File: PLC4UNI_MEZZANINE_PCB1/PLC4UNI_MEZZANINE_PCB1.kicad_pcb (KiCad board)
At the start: 2 copper layers, 29.7 x 37.1 mm, 15 parts, among them J1 PZ254R-12-14P, U1 MC-121-L119

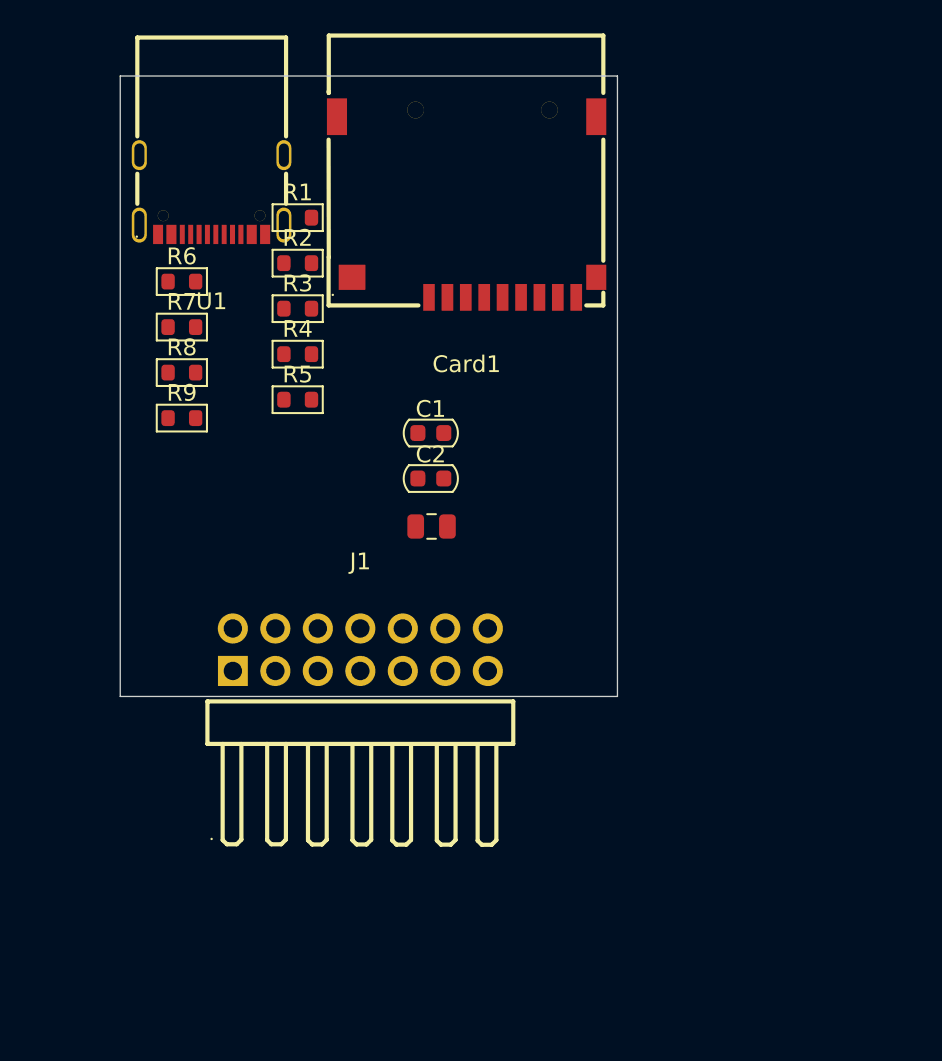
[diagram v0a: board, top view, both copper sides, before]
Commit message: Se cambio el conector J1 de 16 pines por un conector de 18 pines, para poder utilizar el display + touch en modo spi.
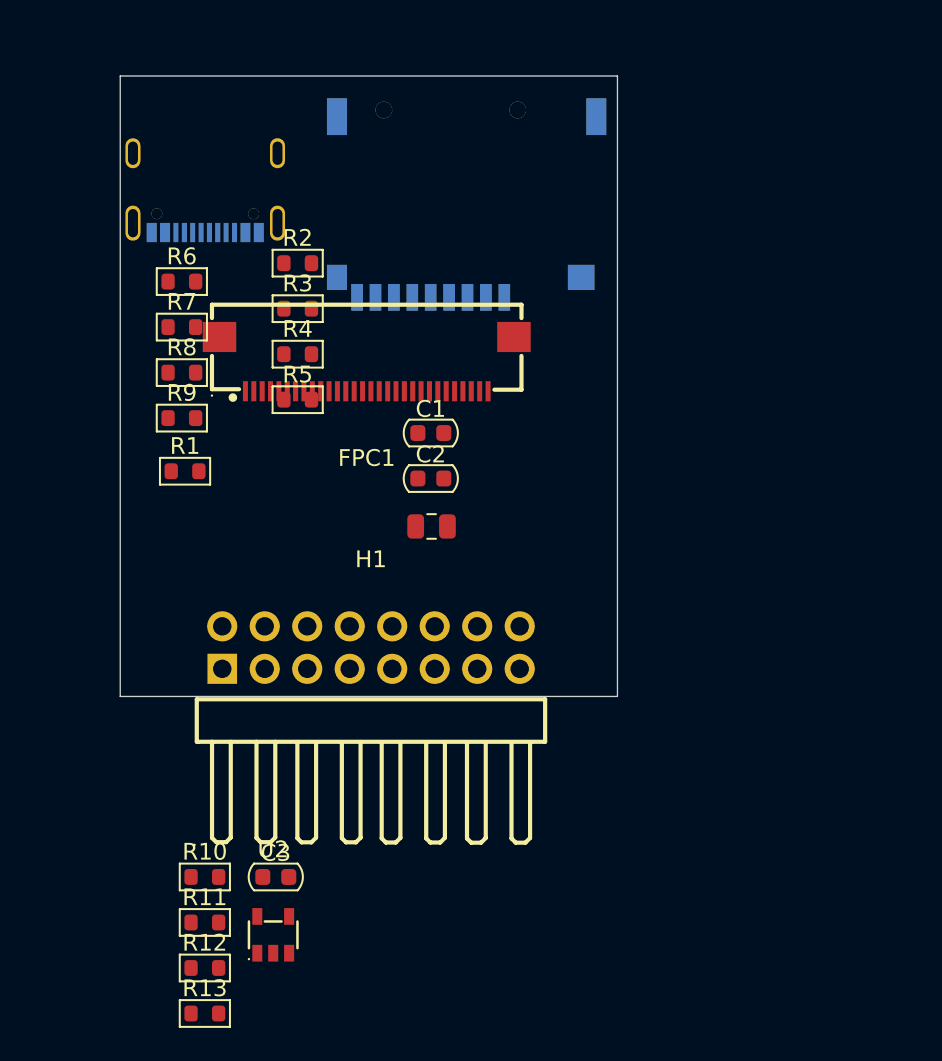
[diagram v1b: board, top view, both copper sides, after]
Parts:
- removed J1: PZ254R-12-14P, EasyEDA:HDR-TH_14P-P2.54-H-M-R2-C7-S2.54
- added C3: 10uF, Capacitor_SMD_AKL:C_0603_1608Metric, F.Cu at (107.6, 112.0)
- added FPC1: FPC-05FB-30PH20, EasyEDA:FPC-SMD_30P-P0.50_FPC-05FB-30PH20, F.Cu at (113.0, 81.4)
- added H1: PZ254R-12-16P, EasyEDA:HDR-TH_16P-P2.54-H-M-R2-C8-S2.54, F.Cu at (113.3, 98.3)
- added R10: 6.8K, Resistor_SMD_AKL:R_0603_1608Metric, F.Cu at (103.4, 112.0)
- added R11: 300, Resistor_SMD_AKL:R_0603_1608Metric, F.Cu at (103.4, 114.7)
- added R12: 5.1k, Resistor_SMD_AKL:R_0603_1608Metric, F.Cu at (103.4, 117.4)
- added R13: 5.1k, Resistor_SMD_AKL:R_0603_1608Metric, F.Cu at (103.4, 120.2)
- added U2: MT9700-N, EasyEDA:SOT-23-5_L2.9-W1.6-P0.95-LS2.9-BL, F.Cu at (107.4, 115.5)
- Card1, U1: moved to B.Cu
- moved R1 16.6 mm to (102.2, 87.8)
- moved U1 0.40 mm to (103.4, 71.1), turned to 0 degrees
- turned Card1 to 0 degrees
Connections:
- net Net-(Card1-CD/DAT3) renamed /sd_cs

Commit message: Avances en esquemas y documentacion
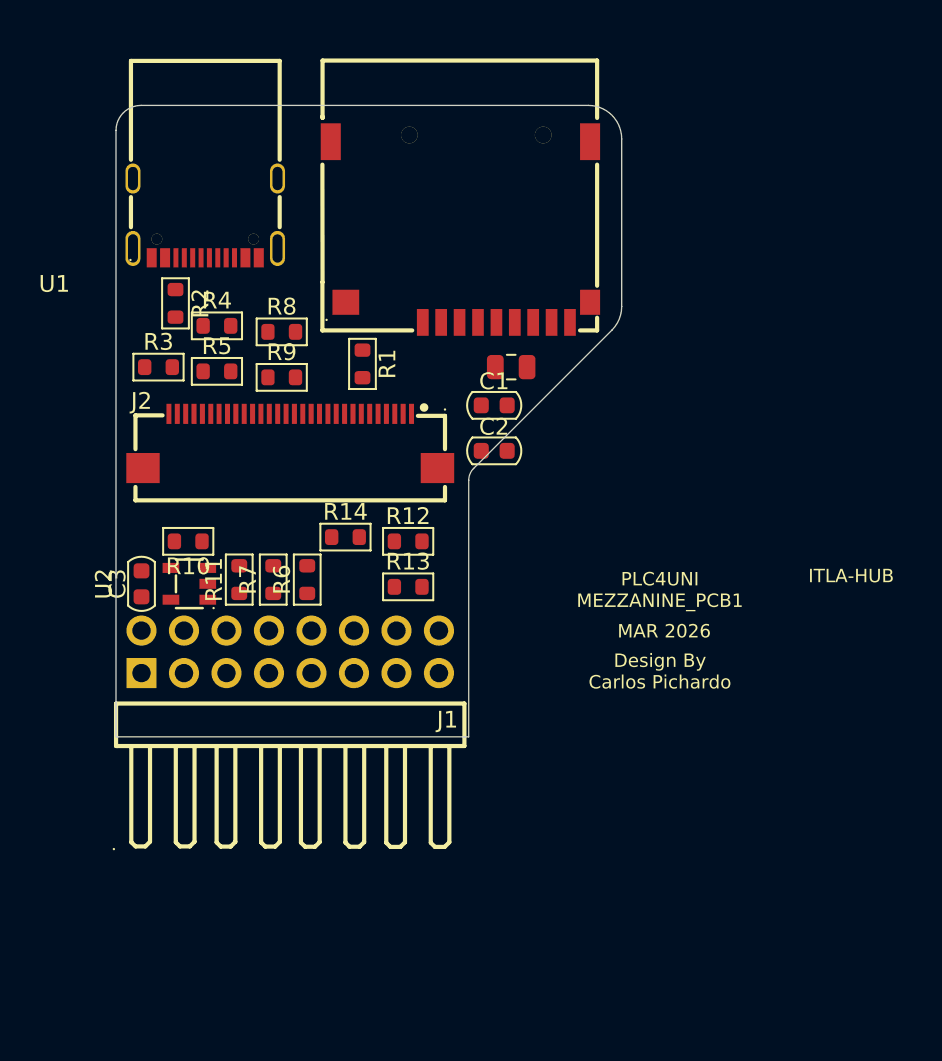
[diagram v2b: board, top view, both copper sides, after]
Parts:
- added R14: 10K, Resistor_SMD_AKL:R_0603_1608Metric, F.Cu at (111.8, 91.7)
- Card1, U1: moved to F.Cu
- R12, R13: value 5.1k -> 10K
- R3: value 10K -> 2.2K
- R4, R8: value 2.2K -> 10K
- moved R12 28.2 mm to (115.5, 91.9)
- moved R13 28.2 mm to (115.5, 94.7)
- moved U2 21.6 mm to (102.4, 94.5), turned to 90 degrees
- moved R11 20.6 mm to (105.4, 94.2), turned to 90 degrees
- moved R10 20.1 mm to (102.4, 91.9), turned to 180 degrees
- moved R6 19.3 mm to (109.5, 94.2), turned to 90 degrees
- moved C3 19.3 mm to (99.6, 94.5), turned to 90 degrees
- moved R7 16.0 mm to (107.4, 94.2), turned to 90 degrees
- moved R1 12.4 mm to (112.8, 81.3), turned to -90 degrees
- moved L1 10.6 mm to (121.7, 81.5)
- moved R3 9.02 mm to (100.6, 81.5)
- moved R2 7.69 mm to (101.6, 77.7), turned to -90 degrees
- moved J2 6.48 mm to (108.5, 85.9), turned to 0 degrees
- moved R8 6.45 mm to (108.0, 79.4)
- moved R9 6.45 mm to (108.0, 82.1)
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- renumbered H1 to J1, FPC1 to J2
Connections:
- Card1 pad 2: /sd_cs -> /SD_CS
- Card1 pad 3: /mosi -> /SPI_MOSI
- R3 pad 2: /mosi -> /SPI_MOSI
- R5 pad 2: /miso -> /SPI_MISO
- R6 pad 1: /clk -> /SPI_CLK
- R7 pad 1: /miso -> /SPI_MISO
- R9 pad 2: /sd_cs -> /SD_CS
- U1 pad A6: /usb+ -> /USB+
- U1 pad A7: /usb- -> /USB-
- U1 pad B6: /usb+ -> /USB+
- U1 pad B7: /usb- -> /USB-
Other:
- board size 29.7 x 37.1 mm -> 30.2 x 37.7 mm
- board text added: "Design By Carlos Pichardo"
- board text added: "ITLA-HUB"
- board text added: "MAR 2026"
- board text added: "PLC4UNI MEZZANINE_PCB1"
